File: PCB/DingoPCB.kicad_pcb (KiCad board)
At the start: 2 copper layers, 80 x 40 mm, 23 parts, among them J1 BATT(~15V), J10 BATT CHECK, J11 1935776, J12 1935776, J13 1935776, J14 1935776, J15 TEMP1, J16 TEMP2, J17 TEMP3, J18 TEMP4, J19 FAN1, J2 PWR1, J20 FAN2, J3 PWR2, J4 PWR3, J5 PWR4, J6 12VIN, J7 5VIN, J8 1935776, J9 1935776

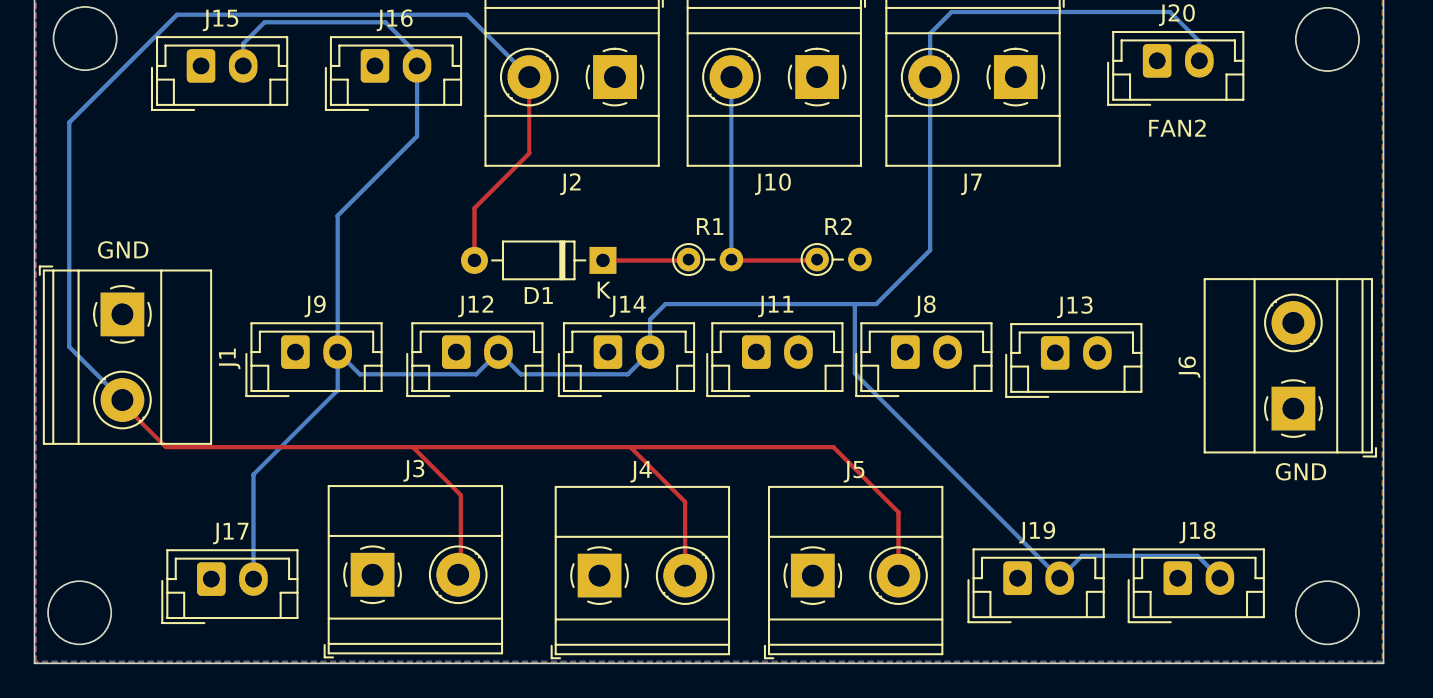
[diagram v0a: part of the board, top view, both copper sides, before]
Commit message: Updates to masks on PCB
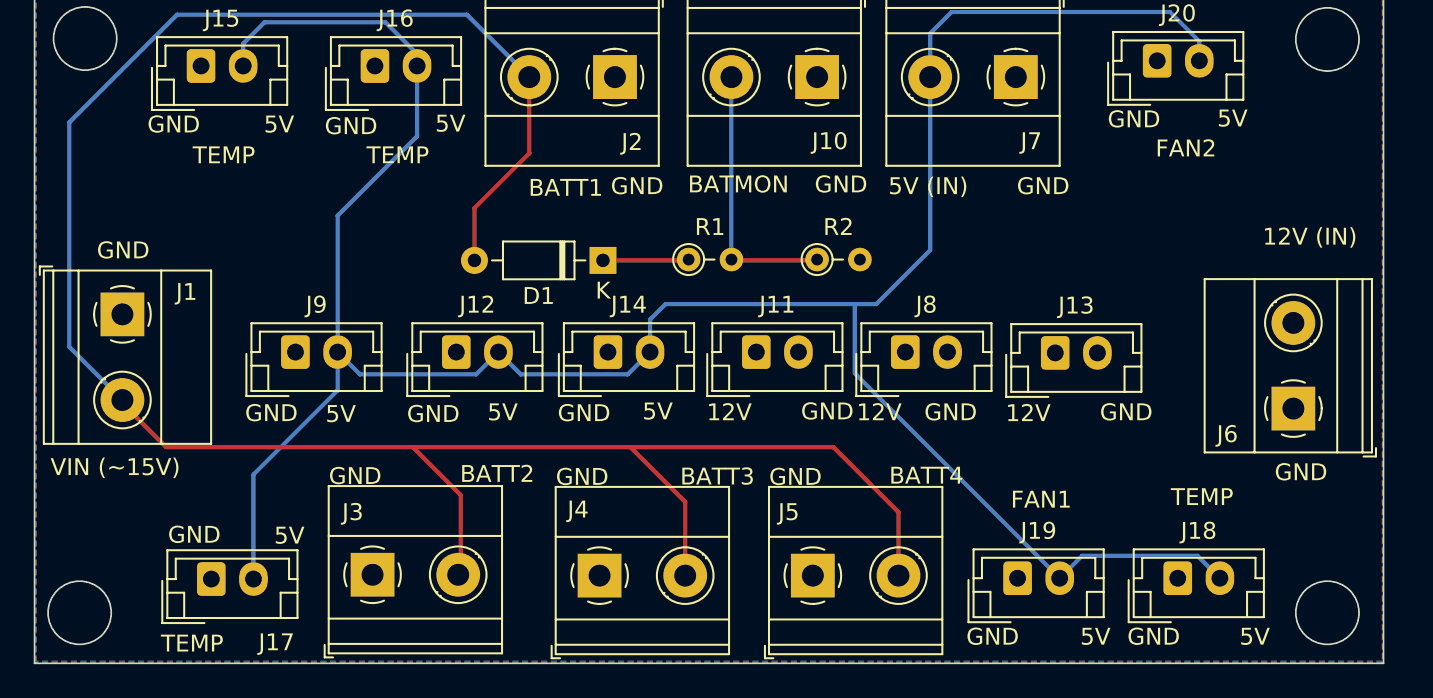
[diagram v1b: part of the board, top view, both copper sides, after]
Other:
- board text added: "12V"
- board text added: "12V (IN)"
- board text added: "5V"
- board text added: "5V (IN)"
- board text added: "BATMON"
- board text added: "BATT1"
- board text added: "BATT2"
- board text added: "BATT3"
- board text added: "BATT4"
- board text added: "FAN1"
- board text added: "TEMP"
- board text added: "VIN (~15V)"
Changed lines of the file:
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@@
     (property "ki_keywords" "connector")
     (attr through_hole)
-    (fp_text reference "J1" (at 2.54 -6.26 90) (layer "F.SilkS")
+    (fp_text reference "J1" (at -1.3208 -3.81 -180) (layer "F.SilkS")
         (effects (font (size 1 1) (thickness 0.15)))
     )
@@
     (property "ki_keywords" "connector")
     (attr through_hole)
-    (fp_text reference "J4" (at 2.54 -6.26) (layer "F.SilkS")
+    (fp_text reference "J4" (at -1.27 -3.9116) (layer "F.SilkS")
         (effects (font (size 1 1) (thickness 0.15)))
     )
@@
     (property "ki_keywords" "connector")
     (attr through_hole)
-    (fp_text reference "J2" (at 2.54 -6.26) (layer "F.SilkS")
+    (fp_text reference "J2" (at -1.016 -3.8608) (layer "F.SilkS")
         (effects (font (size 1 1) (thickness 0.15)))
     )
@@
     (property "ki_keywords" "connector")
     (attr through_hole)
-    (fp_text reference "J7" (at 2.54 -6.26) (layer "F.SilkS")
+    (fp_text reference "J7" (at -0.9144 -3.81) (layer "F.SilkS")
         (effects (font (size 1 1) (thickness 0.15)))
     )
@@
     (property "ki_keywords" "connector")
     (attr through_hole)
-    (fp_text reference "J17" (at 1.25 -2.8) (layer "F.SilkS")
+    (fp_text reference "J17" (at 3.8716 3.7592) (layer "F.SilkS")
         (effects (font (size 1 1) (thickness 0.15)))
     )
@@
     (property "ki_keywords" "connector")
     (attr through_hole)
-    (fp_text reference "J3" (at 2.54 -6.26) (layer "F.SilkS")
+    (fp_text reference "J3" (at -1.1684 -3.7084) (layer "F.SilkS")
         (effects (font (size 1 1) (thickness 0.15)))
     )
@@
     (property "ki_keywords" "connector")
     (attr through_hole)
-    (fp_text reference "J5" (at 2.54 -6.26) (layer "F.SilkS")
+    (fp_text reference "J5" (at -1.4224 -3.7592) (layer "F.SilkS")
         (effects (font (size 1 1) (thickness 0.15)))
     )
@@
     (property "ki_keywords" "connector")
     (attr through_hole)
-    (fp_text reference "J6" (at 2.54 -6.26 90) (layer "F.SilkS")
+    (fp_text reference "J6" (at -1.524 -3.9116 180) (layer "F.SilkS")
         (effects (font (size 1 1) (thickness 0.15)))
     )
@@
     (property "ki_keywords" "connector")
     (attr through_hole)
-    (fp_text reference "J10" (at 2.54 -6.26) (layer "F.SilkS")
-        (effects (font (size 1 1) (thickness 0.15)))
-    )
-    (fp_text value "BATT CHECK" (at 0.9144 -7.1628) (layer "F.Fab")
+    (fp_text reference "J10" (at -0.762 -3.81) (layer "F.SilkS")
+        (effects (font (size 1 1) (thickness 0.15)))
+    )
+    (fp_text value "BATT CHECK" (at 1.9304 -7.6708) (layer "F.Fab") hide
         (effects (font (size 1 1) (thickness 0.15)))
     )
@@
   (gr_circle (center 77 3) (end 78.8741 3)
     (stroke (width 0.1) (type default)) (fill none) (layer "Edge.Cuts"))
+  (gr_text "GND" (at 63.9572 8.3312) (layer "F.SilkS")
+    (effects (font (size 1 1) (thickness 0.15)) (justify left bottom))
+  )
+  (gr_text "VIN (~15V)" (at 1.27 28.956) (layer "F.SilkS")
+    (effects (font (size 1 1) (thickness 0.15)) (justify left bottom))
+  )
+  (gr_text "5V" (at 24.0792 8.5852) (layer "F.SilkS")
+    (effects (font (size 1 1) (thickness 0.15)) (justify left bottom))
+  )
+  (gr_text "GND" (at 55.5752 39.0144) (layer "F.SilkS")
+    (effects (font (size 1 1) (thickness 0.15)) (justify left bottom))
+  )
+  (gr_text "12V" (at 57.912 25.7556) (layer "F.SilkS")
+    (effects (font (size 1 1) (thickness 0.15)) (justify left bottom))
+  )
   (gr_text "GND" (at 4.0132 16.1036) (layer "F.SilkS")
     (effects (font (size 1 1) (thickness 0.15)) (justify left bottom))
   )
+  (gr_text "BATT3" (at 38.608 29.5148) (layer "F.SilkS")
+    (effects (font (size 1 1) (thickness 0.15)) (justify left bottom))
+  )
+  (gr_text "5V (IN)" (at 50.9524 12.2936) (layer "F.SilkS")
+    (effects (font (size 1 1) (thickness 0.15)) (justify left bottom))
+  )
+  (gr_text "GND" (at 43.882 29.537) (layer "F.SilkS")
+    (effects (font (size 1 1) (thickness 0.15)) (justify left bottom))
+  )
+  (gr_text "GND" (at 22.4028 25.8064) (layer "F.SilkS")
+    (effects (font (size 1 1) (thickness 0.15)) (justify left bottom))
+  )
+  (gr_text "GND" (at 63.5 25.7048) (layer "F.SilkS")
+    (effects (font (size 1 1) (thickness 0.15)) (justify left bottom))
+  )
+  (gr_text "TEMP" (at 20.0152 10.4648) (layer "F.SilkS")
+    (effects (font (size 1 1) (thickness 0.15)) (justify left bottom))
+  )
+  (gr_text "5V" (at 27.178 25.7048) (layer "F.SilkS")
+    (effects (font (size 1 1) (thickness 0.15)) (justify left bottom))
+  )
+  (gr_text "GND" (at 7.0104 8.636) (layer "F.SilkS")
+    (effects (font (size 1 1) (thickness 0.15)) (justify left bottom))
+  )
+  (gr_text "12V (IN)" (at 73.152 15.2908) (layer "F.SilkS")
+    (effects (font (size 1 1) (thickness 0.15)) (justify left bottom))
+  )
   (gr_text "GND" (at 73.8632 29.2608) (layer "F.SilkS")
     (effects (font (size 1 1) (thickness 0.15)) (justify left bottom))
   )
-  (gr_text "FAN2" (at 66.294 8.89) (layer "F.SilkS")
-    (effects (font (size 1 1) (thickness 0.15)) (justify left bottom))
-  )
+  (gr_text "GND" (at 17.526 8.7376) (layer "F.SilkS")
+    (effects (font (size 1 1) (thickness 0.15)) (justify left bottom))
+  )
+  (gr_text "GND" (at 58.5724 12.2936) (layer "F.SilkS")
+    (effects (font (size 1 1) (thickness 0.15)) (justify left bottom))
+  )
+  (gr_text "5V" (at 70.4596 8.2804) (layer "F.SilkS")
+    (effects (font (size 1 1) (thickness 0.15)) (justify left bottom))
+  )
+  (gr_text "5V" (at 71.7804 39.0144) (layer "F.SilkS")
+    (effects (font (size 1 1) (thickness 0.15)) (justify left bottom))
+  )
+  (gr_text "BATT4" (at 51.0032 29.464) (layer "F.SilkS")
+    (effects (font (size 1 1) (thickness 0.15)) (justify left bottom))
+  )
+  (gr_text "TEMP" (at 67.7164 30.734) (layer "F.SilkS")
+    (effects (font (size 1 1) (thickness 0.15)) (justify left bottom))
+  )
+  (gr_text "GND" (at 45.7708 25.654) (layer "F.SilkS")
+    (effects (font (size 1 1) (thickness 0.15)) (justify left bottom))
+  )
+  (gr_text "5V" (at 62.3316 39.0144) (layer "F.SilkS")
+    (effects (font (size 1 1) (thickness 0.15)) (justify left bottom))
+  )
+  (gr_text "FAN1" (at 58.2168 30.8864) (layer "F.SilkS")
+    (effects (font (size 1 1) (thickness 0.15)) (justify left bottom))
+  )
+  (gr_text "GND" (at 46.5836 12.192) (layer "F.SilkS")
+    (effects (font (size 1 1) (thickness 0.15)) (justify left bottom))
+  )
+  (gr_text "5V" (at 36.3728 25.654) (layer "F.SilkS")
+    (effects (font (size 1 1) (thickness 0.15)) (justify left bottom))
+  )
+  (gr_text "GND" (at 65.1256 39.0144) (layer "F.SilkS")
+    (effects (font (size 1 1) (thickness 0.15)) (justify left bottom))
+  )
+  (gr_text "BATMON" (at 39.0652 12.192) (layer "F.SilkS")
+    (effects (font (size 1 1) (thickness 0.15)) (justify left bottom))
+  )
+  (gr_text "12V" (at 40.1828 25.7048) (layer "F.SilkS")
+    (effects (font (size 1 1) (thickness 0.15)) (justify left bottom))
+  )
+  (gr_text "BATT1" (at 29.6164 12.3952) (layer "F.SilkS")
+    (effects (font (size 1 1) (thickness 0.15)) (justify left bottom))
+  )
+  (gr_text "GND" (at 34.4932 12.2936) (layer "F.SilkS")
+    (effects (font (size 1 1) (thickness 0.15)) (justify left bottom))
+  )
+  (gr_text "5V" (at 17.5768 25.8064) (layer "F.SilkS")
+    (effects (font (size 1 1) (thickness 0.15)) (justify left bottom))
+  )
+  (gr_text "5V" (at 13.9192 8.636) (layer "F.SilkS")
+    (effects (font (size 1 1) (thickness 0.15)) (justify left bottom))
+  )
+  (gr_text "GND" (at 53.086 25.7048) (layer "F.SilkS")
+    (effects (font (size 1 1) (thickness 0.15)) (justify left bottom))
+  )
+  (gr_text "GND" (at 12.8016 25.7556) (layer "F.SilkS")
+    (effects (font (size 1 1) (thickness 0.15)) (justify left bottom))
+  )
+  (gr_text "GND" (at 31.2328 29.537) (layer "F.SilkS")
+    (effects (font (size 1 1) (thickness 0.15)) (justify left bottom))
+  )
+  (gr_text "FAN2" (at 66.802 10.0584) (layer "F.SilkS")
+    (effects (font (size 1 1) (thickness 0.15)) (justify left bottom))
+  )
+  (gr_text "TEMP" (at 7.8232 39.4208) (layer "F.SilkS")
+    (effects (font (size 1 1) (thickness 0.15)) (justify left bottom))
+  )
+  (gr_text "BATT2" (at 25.5524 29.3624) (layer "F.SilkS")
+    (effects (font (size 1 1) (thickness 0.15)) (justify left bottom))
+  )
+  (gr_text "GND" (at 8.2296 32.9692) (layer "F.SilkS")
+    (effects (font (size 1 1) (thickness 0.15)) (justify left bottom))
+  )
+  (gr_text "GND" (at 31.3436 25.7556) (layer "F.SilkS")
+    (effects (font (size 1 1) (thickness 0.15)) (justify left bottom))
+  )
+  (gr_text "5V" (at 14.5288 33.02) (layer "F.SilkS")
+    (effects (font (size 1 1) (thickness 0.15)) (justify left bottom))
+  )
+  (gr_text "TEMP" (at 9.7028 10.4648) (layer "F.SilkS")
+    (effects (font (size 1 1) (thickness 0.15)) (justify left bottom))
+  )
+  (gr_text "GND" (at 17.7708 29.4862) (layer "F.SilkS")
+    (effects (font (size 1 1) (thickness 0.15)) (justify left bottom))
+  )
+  (gr_text "12V" (at 49.0728 25.7048) (layer "F.SilkS")
+    (effects (font (size 1 1) (thickness 0.15)) (justify left bottom))
+  )

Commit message: Gerber files added
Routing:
- net +15V: track 132.8 -> 0.00 mm
- net +12V: track 0.00 -> 36.4 mm
- added copper zone on F.Cu, net +15V
- removed copper zone on F.Cu, net +12V
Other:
- board text added: "UNOFFICIAL DINGO PCB"

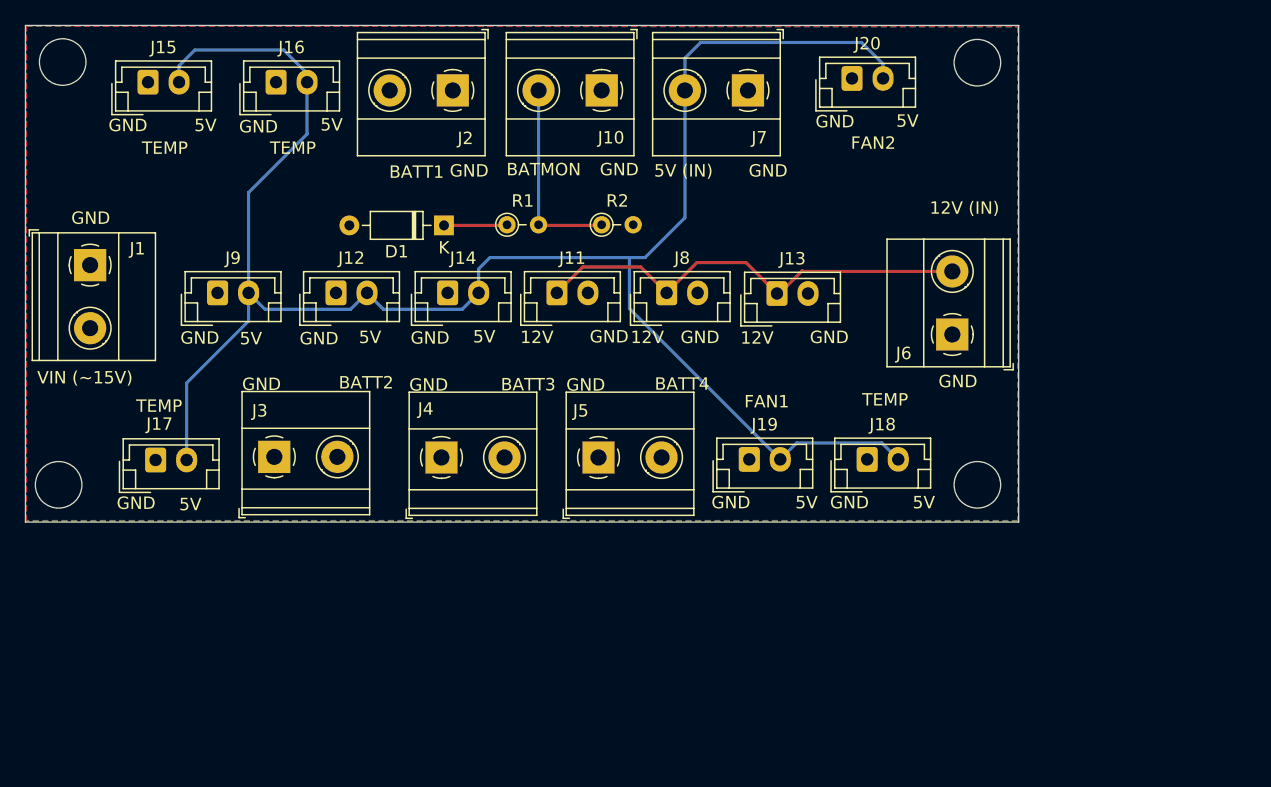
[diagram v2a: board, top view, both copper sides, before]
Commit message: Moved terminals closer together
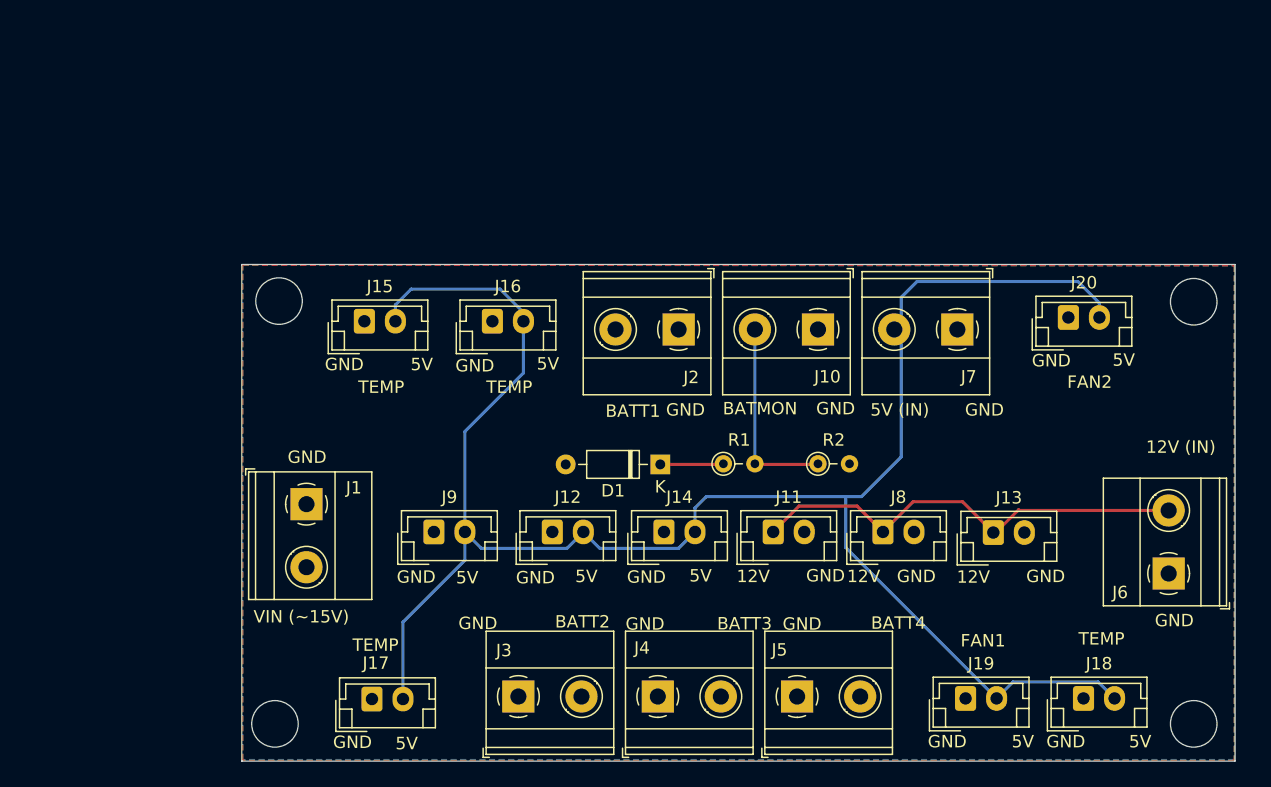
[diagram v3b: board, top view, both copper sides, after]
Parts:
- moved J3 27.6 mm to (40.0, 54.1)
- moved J2 26.5 mm to (52.9, 24.5)
- moved J11 26.0 mm to (60.6, 40.8)
- moved J18 26.0 mm to (85.5, 54.2)
- moved J19 26.0 mm to (76.0, 54.2)
- moved J20 26.0 mm to (84.3, 23.5)
- moved D1 26.0 mm to (51.5, 35.4)
- moved J1 26.0 mm to (23.0, 38.6)
- moved J10 26.0 mm to (64.2, 24.5)
- moved J12 26.0 mm to (42.8, 40.8)
- moved J13 26.0 mm to (78.3, 40.8)
- moved J14 26.0 mm to (51.8, 40.8)
- moved J15 26.0 mm to (27.6, 23.8)
- moved J16 26.0 mm to (37.9, 23.8)
- moved J17 26.0 mm to (28.2, 54.3)
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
